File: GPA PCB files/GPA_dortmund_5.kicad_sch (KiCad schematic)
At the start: 29 parts, among them U103 AAVID_TO220_HEATSINK, U23 OPA549_KV_11TO-220_11, U24 OPA549_KV_11TO-220_11, U25 INA149SOIC8, X9 MINI-FIT-JR-045569-NA2

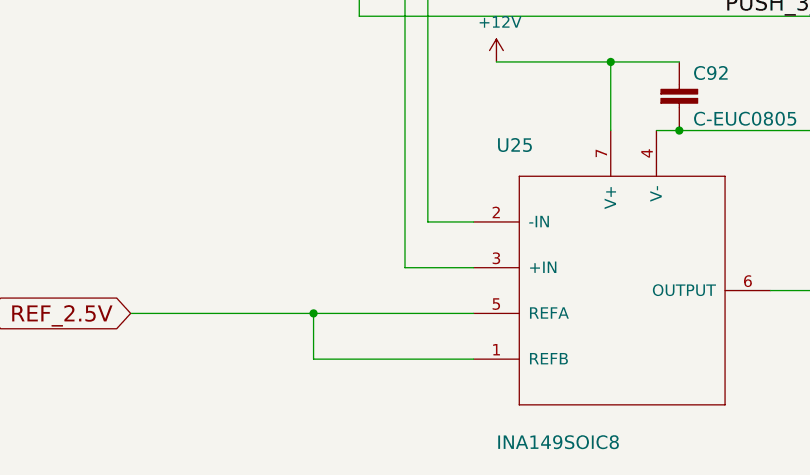
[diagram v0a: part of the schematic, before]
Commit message: converted symbol library to KiCad6 (.kicad_sym)
fixed some pin types to clear ERC and DRC errors/warnings;
added solder jumper to switch from INA149 to LT1990A
fixed layer boundaries (some artifacts from the eagle conversion
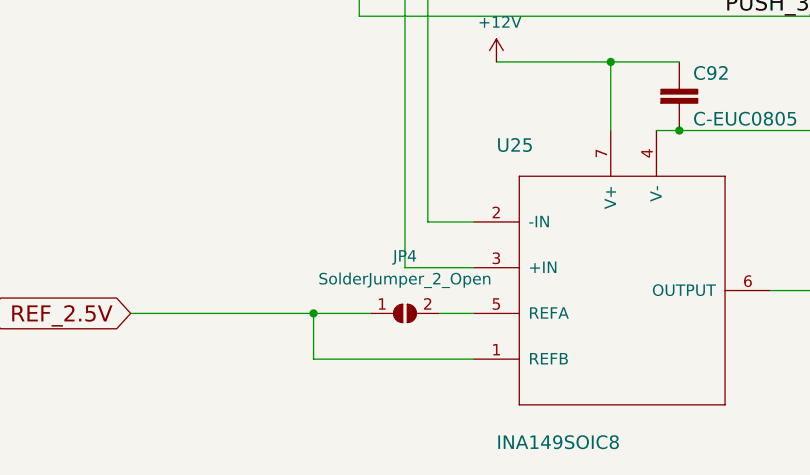
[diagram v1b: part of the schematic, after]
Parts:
- added JP4: SolderJumper_2_Open, Jumper:SolderJumper-2_P1.3mm_Open_RoundedPad1.0x1.5mm, symbol Jumper:SolderJumper_2_Open
- U23, U24: symbol GPA_dortmund-rescue:OPA549_KV_11TO-220_11-GPA_dortmund-eagle-import -> GPA_dortmund-eagle-import:OPA549_KV_11TO-220_11
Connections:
- net REF_2.5V: now also JP4.1 (A); no longer U25.5 (REFA)
- new net: JP4.2 (B), U25.5 (REFA)
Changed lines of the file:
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@@
+    (stroke (width 0) (type default) (color 0 0 0 0))
+  )
+  (wire (pts (xy 148.59 172.72) (xy 142.24 172.72))
     (stroke (width 0) (type default) (color 0 0 0 0))
   )
@@
     (stroke (width 0) (type default) (color 0 0 0 0))
   )
-  (wire (pts (xy 160.02 172.72) (xy 142.24 172.72))
+  (wire (pts (xy 160.02 172.72) (xy 156.21 172.72))
     (stroke (width 0) (type default) (color 0 0 0 0))
   )
@@
     (pin "2")
   )
-  (symbol (lib_id "GPA_dortmund-rescue:OPA549_KV_11TO-220_11-GPA_dortmund-eagle-import") (at 119.38 96.52 0) (unit 1)
+  (symbol (lib_id "GPA_dortmund-eagle-import:OPA549_KV_11TO-220_11") (at 119.38 96.52 0) (unit 1)
     (in_bom yes) (on_board yes)
     (property "Reference" "U23" (id 0) (at 127.3556 89.9414 0)
@@
       (effects (font (size 1.27 1.27)) hide)
     )
+    (pin "8")
     (pin "1")
     (pin "2")
@@
     (pin "7")
   )
-  (symbol (lib_id "GPA_dortmund-rescue:OPA549_KV_11TO-220_11-GPA_dortmund-eagle-import") (at 200.66 96.52 0) (mirror y) (unit 1)
+  (symbol (lib_id "GPA_dortmund-eagle-import:OPA549_KV_11TO-220_11") (at 200.66 96.52 0) (mirror y) (unit 1)
     (in_bom yes) (on_board yes)
     (property "Reference" "U24" (id 0) (at 177.4444 89.9414 0)
@@
       (effects (font (size 1.27 1.27)) hide)
     )
+    (pin "1")
+    (pin "2")
+  )
+  (symbol (lib_id "Jumper:SolderJumper_2_Open") (at 152.4 172.72 0) (unit 1)
+    (in_bom yes) (on_board yes) (fields_autoplaced)
+    (property "Reference" "JP4" (id 0) (at 152.4 166.37 0))
+    (property "Value" "SolderJumper_2_Open" (id 1) (at 152.4 168.91 0))
+    (property "Footprint" "Jumper:SolderJumper-2_P1.3mm_Open_RoundedPad1.0x1.5mm" (id 2) (at 152.4 172.72 0)
+      (effects (font (size 1.27 1.27)) hide)
+    )
+    (property "Datasheet" "~" (id 3) (at 152.4 172.72 0)
+      (effects (font (size 1.27 1.27)) hide)
+    )

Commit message: added 3D models + footprint changes
changed footprints of OPA549T bulk capacitors
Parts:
- C87, C88, C90, C91: footprint GPA_dortmund:C0805 -> Capacitor_SMD:C_1210_3225Metric_Pad1.33x2.70mm_HandSolder
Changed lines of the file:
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@@
       (effects (font (size 1.4986 1.4986)) (justify left bottom))
     )
-    (property "Footprint" "GPA_dortmund:C0805" (id 2) (at 121.92 38.1 0)
+    (property "Footprint" "Capacitor_SMD:C_1210_3225Metric_Pad1.33x2.70mm_HandSolder" (id 2) (at 121.92 38.1 0)
       (effects (font (size 1.27 1.27)) hide)
     )
@@
       (effects (font (size 1.4986 1.4986)) (justify left bottom))
     )
-    (property "Footprint" "GPA_dortmund:C0805" (id 2) (at 193.04 38.1 0)
+    (property "Footprint" "Capacitor_SMD:C_1210_3225Metric_Pad1.33x2.70mm_HandSolder" (id 2) (at 193.04 38.1 0)
       (effects (font (size 1.27 1.27)) hide)
     )
@@
       (effects (font (size 1.4986 1.4986)) (justify left bottom))
     )
-    (property "Footprint" "GPA_dortmund:C0805" (id 2) (at 132.08 38.1 0)
+    (property "Footprint" "Capacitor_SMD:C_1210_3225Metric_Pad1.33x2.70mm_HandSolder" (id 2) (at 132.08 38.1 0)
       (effects (font (size 1.27 1.27)) hide)
     )
@@
       (effects (font (size 1.4986 1.4986)) (justify left bottom))
     )
-    (property "Footprint" "GPA_dortmund:C0805" (id 2) (at 203.2 38.1 0)
-      (effects (font (size 1.27 1.27)) hide)
-    )
+    (property "Footprint" "Capacitor_SMD:C_1210_3225Metric_Pad1.33x2.70mm_HandSolder" (id 2) (at 203.2 38.1 0)
+      (effects (font (size 1.27 1.27)) hide)
+    )
